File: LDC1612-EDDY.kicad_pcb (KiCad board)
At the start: 2 copper layers, 38 x 21 mm, 12 parts, among them J1 Conn_01x04_Pin, J2 Conn_01x02_Pin, U1 LDC1612, U2 XC6206P332MR

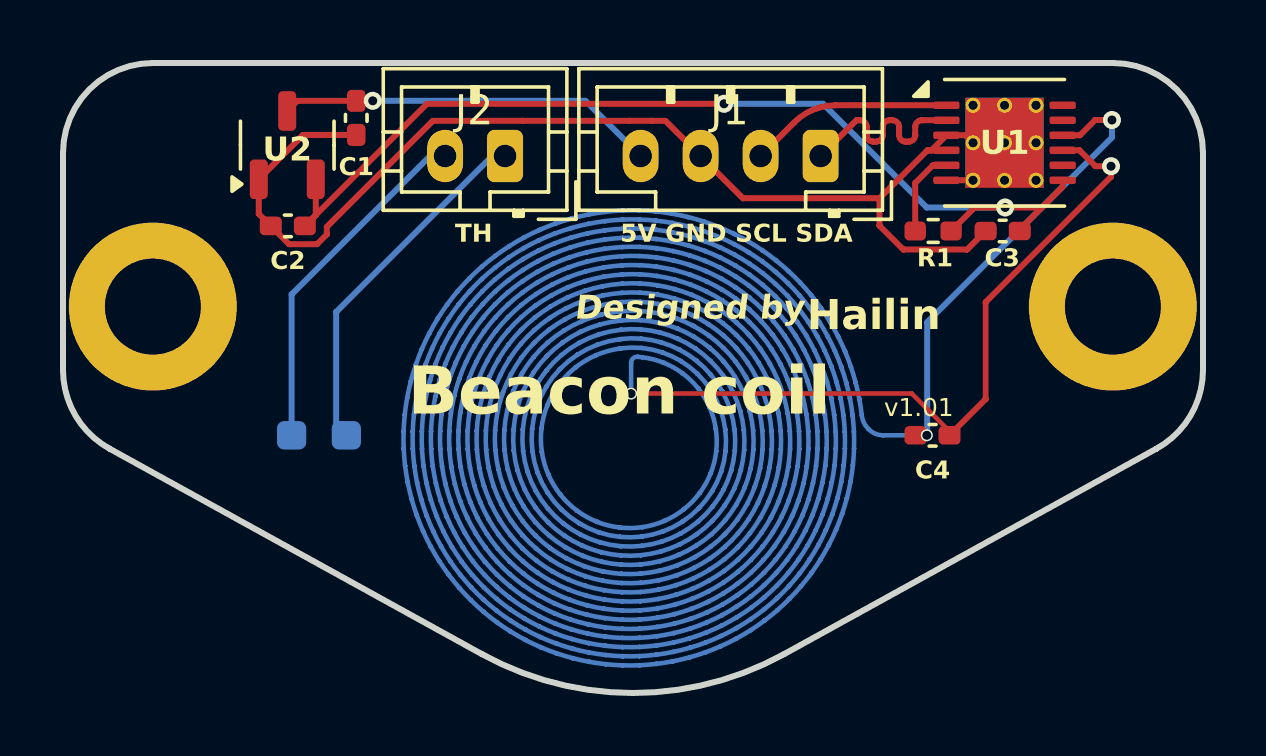
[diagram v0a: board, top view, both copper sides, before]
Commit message: PCB: bump version to v1.02 * add pull-up resistors for SDA & SCL * change board name to `LDC1612 coil`
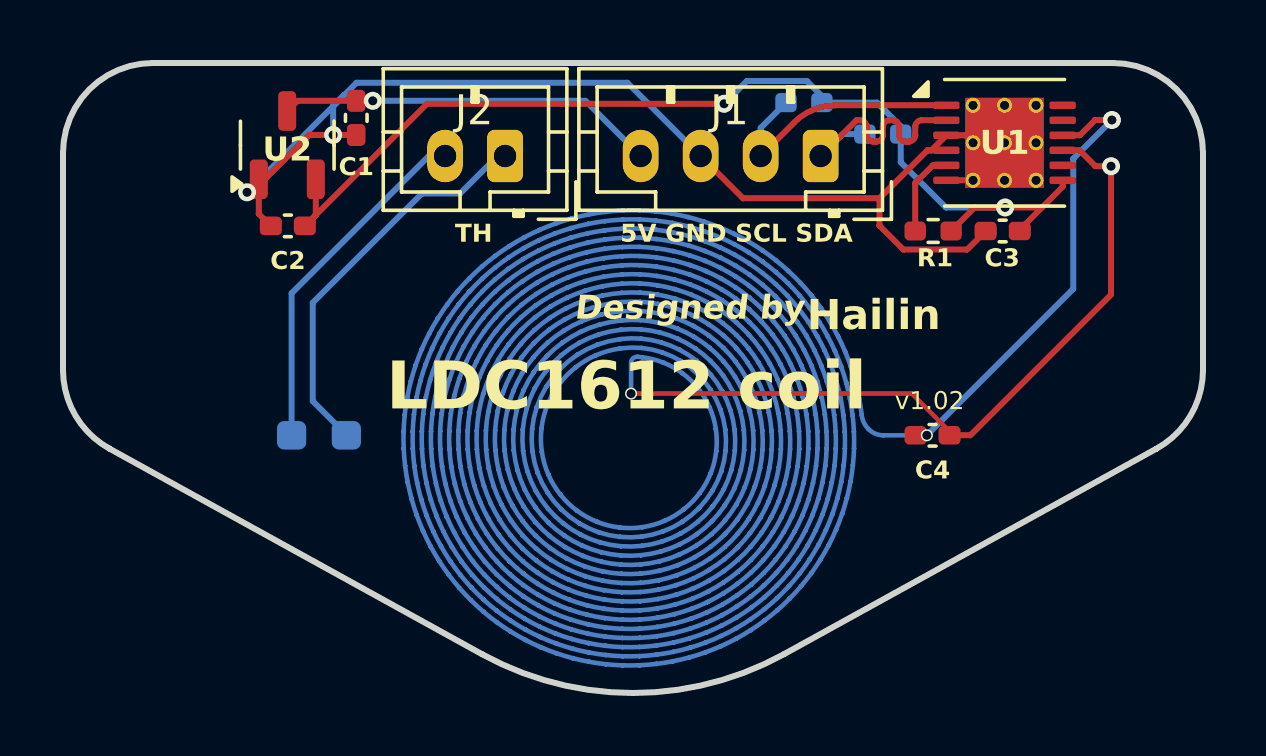
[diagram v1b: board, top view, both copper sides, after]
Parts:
- removed ? (x2): , 
- added R2: 10K, Resistor_SMD:R_0402_1005Metric_Pad0.72x0.64mm_HandSolder, B.Cu at (158.3, 61.3)
- added R3: 10K, Resistor_SMD:R_0402_1005Metric_Pad0.72x0.64mm_HandSolder, B.Cu at (155.7, 60.2)
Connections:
- net /EDDY_TEMP renamed /EDDY_TH
- J2 pad 2: GND -> TH_GND
- TH1 pad 1: GND -> TH_GND
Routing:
- net TH_GND: track 0.00 -> 12.2 mm
- net GND: track 51.4 -> 42.5 mm, vias 0 -> 2
- net /EDDY_TH: track 12.0 -> 14.2 mm
- net /SCL: track 6.80 -> 8.93 mm
- net /SDA: track 6.71 -> 8.49 mm
- net +3.3V: track 33.8 -> 35.3 mm
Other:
- board text added: "LDC1612 coil"
- board text added: "v1.02"
- board text removed: "Beacon coil"
- board text removed: "JLCJLCJLCJLC"
- board text removed: "v1.01"

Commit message: Schematic & PCB: bump version to v1.1 * added an 12MHz external oscillator * fixed LDC1612 GND pin does not connected
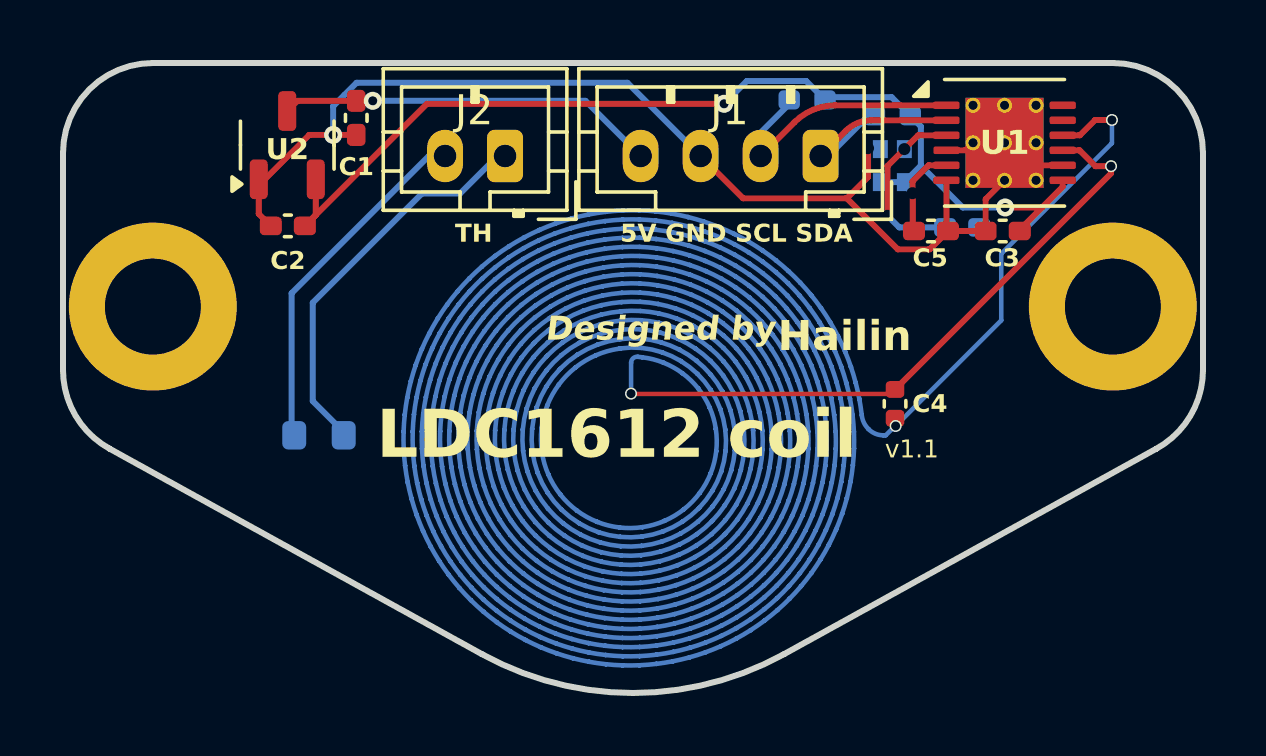
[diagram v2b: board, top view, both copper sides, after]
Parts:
- removed R3: 10K, Resistor_SMD:R_0402_1005Metric_Pad0.72x0.64mm_HandSolder
- added C5: 0.1uF, Capacitor_SMD:C_0402_1005Metric_Pad0.74x0.62mm_HandSolder, F.Cu at (159.9, 64.5)
- added C6: 15pF C0G/NP0, Capacitor_SMD:C_0402_1005Metric_Pad0.74x0.62mm_HandSolder, B.Cu at (160.9, 64.4)
- added REF**: MountingHole_3.2mm_M3_DIN965_Pad, MountingHole:MountingHole_3.2mm_M3_DIN965_Pad, F.Cu at (166.0, 67.0)
- added REF**: MountingHole_3.2mm_M3_DIN965_Pad, MountingHole:MountingHole_3.2mm_M3_DIN965_Pad, F.Cu at (134.0, 67.0)
- added Y1: 12MHz, Oscillator:Oscillator_SMD_Abracon_ASCO-4Pin_1.6x1.2mm, B.Cu at (158.6, 62.3)
- C4: value 330pF -> 56pF C0G/NP0; footprint Capacitor_SMD:C_0402_1005Metric_Pad0.74x0.62mm_HandSolder -> Capacitor_SMD:C_0402_1005Metric
- R1: moved to B.Cu
- TH1: footprint Resistor_SMD:R_0603_1608Metric_Pad0.98x0.95mm_HandSolder -> Resistor_SMD:R_0603_1608Metric
- moved R1 4.07 mm to (158.6, 60.7)
- moved R2 2.77 mm to (155.8, 60.1)
- moved C4 1.63 mm to (158.7, 70.3), turned to -90 degrees
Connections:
- R1 pad 1: Net-(U1-INTB) -> /SDA
- R2 pad 1: /SDA -> /SCL
- U1 pad 3: GND -> Net-(U1-CLKIN)
- U1 pad 5: Net-(U1-INTB) -> +3.3V
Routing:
- net Net-(U1-CLKIN): track 0.00 -> 6.13 mm, vias 0 -> 2
- net /IN0: track 580.3 -> 575.7 mm
- net +3.3V: track 35.3 -> 38.5 mm, vias 2 -> 3
- net Net-(U1-INTB): track 2.89 -> 0.00 mm
- net GND: track 42.5 -> 40.5 mm
- net /SDA: track 8.49 -> 7.48 mm
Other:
- board text added: "v1.1"
- board text removed: "v1.02"

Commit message: release no oscillator version
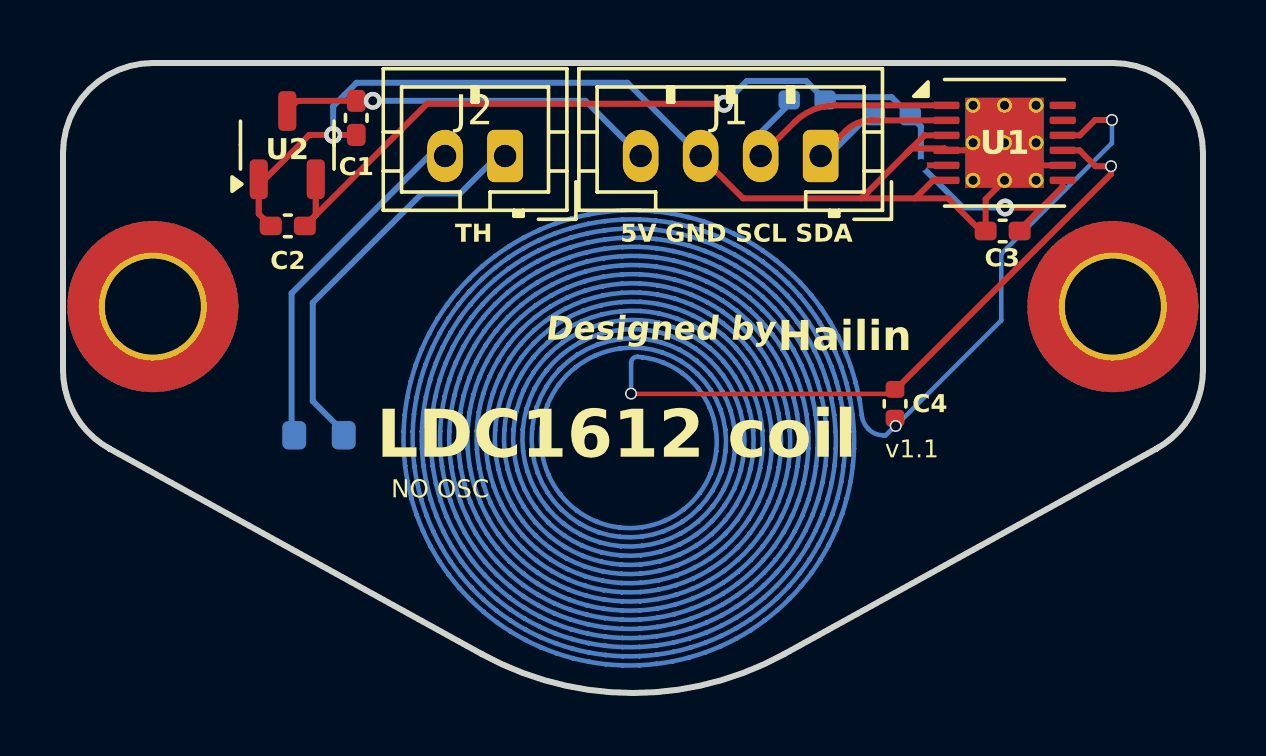
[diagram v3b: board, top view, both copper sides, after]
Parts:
- removed C5: 0.1uF, Capacitor_SMD:C_0402_1005Metric_Pad0.74x0.62mm_HandSolder
- removed C6: 15pF C0G/NP0, Capacitor_SMD:C_0402_1005Metric_Pad0.74x0.62mm_HandSolder
- removed the REF** at (166.0, 67.0)
- removed the REF** at (134.0, 67.0)
- removed Y1: 12MHz, Oscillator:Oscillator_SMD_Abracon_ASCO-4Pin_1.6x1.2mm
- added REF**: MountingHole_3.2mm_M3_ISO7380_Pad_TopBottom, MountingHole:MountingHole_3.2mm_M3_ISO7380_Pad_TopBottom, F.Cu at (134.0, 67.0)
- added REF**: MountingHole_3.2mm_M3_ISO7380_Pad_TopBottom, MountingHole:MountingHole_3.2mm_M3_ISO7380_Pad_TopBottom, F.Cu at (166.0, 67.0)
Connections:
- U1 pad 3: Net-(U1-CLKIN) -> GND
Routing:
- net Net-(U1-CLKIN): track 6.13 -> 0.00 mm, vias 2 -> 0
- net +3.3V: track 38.5 -> 34.2 mm
- net GND: track 40.5 -> 42.3 mm, vias 2 -> 1
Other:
- board text added: "NO OSC"
